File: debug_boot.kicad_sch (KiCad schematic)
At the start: 11 parts, among them J3 Conn_ARM_JTAG_SWD_10, J4 Conn_01x03, J5 Conn_01x05, J6 Conn_01x03, J8 DE9_Pins

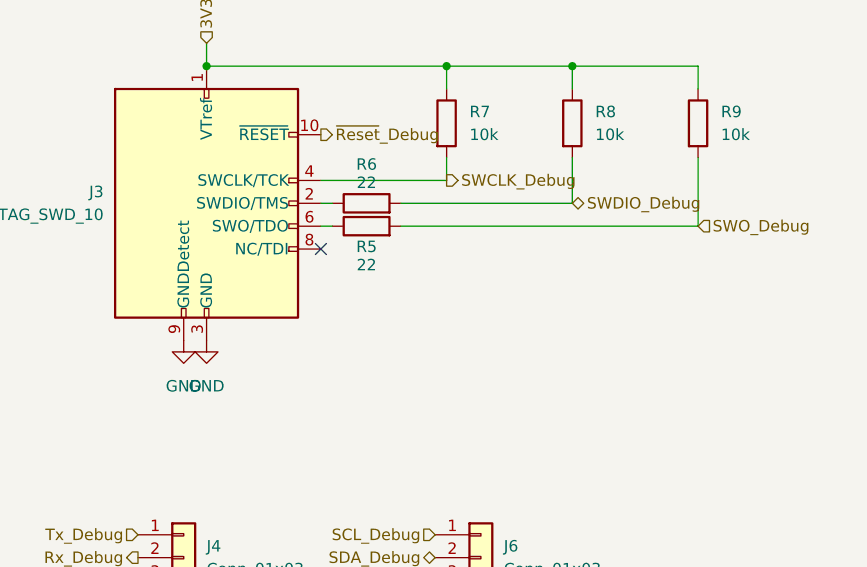
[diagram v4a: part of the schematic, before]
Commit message: Add crystal oscillator and button for reset
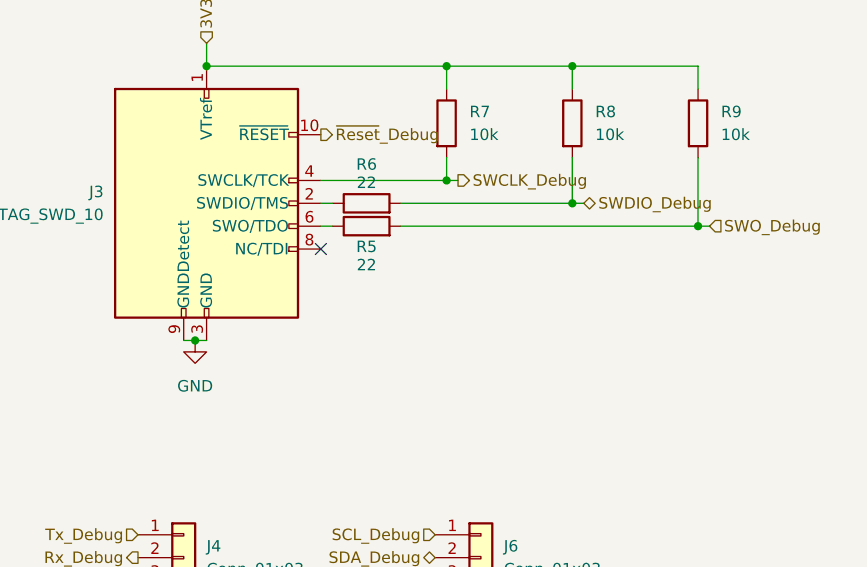
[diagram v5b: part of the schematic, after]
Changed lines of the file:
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@@
+	)
+	(junction
+		(at 172.72 69.85)
+		(diameter 0)
+		(color 0 0 0 0)
 	)
 	(junction
@@
 	)
 	(junction
+		(at 186.69 72.39)
+		(diameter 0)
+		(color 0 0 0 0)
+	)
+	(junction
+		(at 158.75 67.31)
+		(diameter 0)
+		(color 0 0 0 0)
+	)
+	(junction
 		(at 168.91 134.62)
 		(diameter 0)
@@
 	)
 	(junction
+		(at 130.81 85.09)
+		(diameter 0)
+		(color 0 0 0 0)
+	)
+	(junction
 		(at 158.75 54.61)
 		(diameter 0)
@@
 	(wire
 		(pts
+			(xy 172.72 69.85) (xy 172.72 64.77)
+		)
+		(stroke
+			(width 0)
+			(type default)
+		)
+	)
+	(wire
+		(pts
+			(xy 158.75 67.31) (xy 160.02 67.31)
+		)
+		(stroke
+			(width 0)
+			(type default)
+		)
+	)
+	(wire
+		(pts
 			(xy 158.75 54.61) (xy 172.72 54.61)
 		)
@@
 	(wire
 		(pts
+			(xy 162.56 144.78) (xy 168.91 144.78)
+		)
+		(stroke
+			(width 0)
+			(type default)
+		)
+	)
+	(wire
+		(pts
+			(xy 158.75 64.77) (xy 158.75 67.31)
+		)
+		(stroke
+			(width 0)
+			(type default)
+		)
+	)
+	(wire
+		(pts
+			(xy 168.91 144.78) (xy 171.45 144.78)
+		)
+		(stroke
+			(width 0)
+			(type default)
+		)
+	)
+	(wire
+		(pts
+			(xy 168.91 143.51) (xy 168.91 144.78)
+		)
+		(stroke
+			(width 0)
+			(type default)
+		)
+	)
+	(wire
+		(pts
+			(xy 187.96 72.39) (xy 186.69 72.39)
+		)
+		(stroke
+			(width 0)
+			(type default)
+		)
+	)
+	(wire
+		(pts
+			(xy 162.56 134.62) (xy 168.91 134.62)
+		)
+		(stroke
+			(width 0)
+			(type default)
+		)
+	)
+	(wire
+		(pts
+			(xy 132.08 52.07) (xy 132.08 54.61)
+		)
+		(stroke
+			(width 0)
+			(type default)
+		)
+	)
+	(wire
+		(pts
+			(xy 158.75 67.31) (xy 144.78 67.31)
+		)
+		(stroke
+			(width 0)
+			(type default)
+		)
+	)
+	(wire
+		(pts
+			(xy 186.69 72.39) (xy 186.69 64.77)
+		)
+		(stroke
+			(width 0)
+			(type default)
+		)
+	)
+	(wire
+		(pts
+			(xy 171.45 138.43) (xy 180.34 138.43)
+		)
+		(stroke
+			(width 0)
+			(type default)
+		)
+	)
+	(wire
+		(pts
+			(xy 172.72 54.61) (xy 186.69 54.61)
+		)
+		(stroke
+			(width 0)
+			(type default)
+		)
+	)
+	(wire
+		(pts
+			(xy 158.75 54.61) (xy 158.75 57.15)
+		)
+		(stroke
+			(width 0)
+			(type default)
+		)
+	)
+	(wire
+		(pts
+			(xy 130.81 85.09) (xy 129.54 85.09)
+		)
+		(stroke
+			(width 0)
+			(type default)
+		)
+	)
+	(wire
+		(pts
+			(xy 171.45 144.78) (xy 171.45 140.97)
+		)
+		(stroke
+			(width 0)
+			(type default)
+		)
+	)
+	(wire
+		(pts
 			(xy 172.72 69.85) (xy 153.67 69.85)
 		)
@@
 	(wire
 		(pts
-			(xy 186.69 72.39) (xy 186.69 64.77)
-		)
-		(stroke
-			(width 0)
-			(type default)
-		)
-	)
-	(wire
-		(pts
-			(xy 162.56 144.78) (xy 168.91 144.78)
-		)
-		(stroke
-			(width 0)
-			(type default)
-		)
-	)
-	(wire
-		(pts
-			(xy 158.75 64.77) (xy 158.75 67.31)
-		)
-		(stroke
-			(width 0)
-			(type default)
-		)
-	)
-	(wire
-		(pts
-			(xy 168.91 144.78) (xy 171.45 144.78)
-		)
-		(stroke
-			(width 0)
-			(type default)
-		)
-	)
-	(wire
-		(pts
-			(xy 168.91 143.51) (xy 168.91 144.78)
-		)
-		(stroke
-			(width 0)
-			(type default)
-		)
-	)
-	(wire
-		(pts
-			(xy 162.56 134.62) (xy 168.91 134.62)
-		)
-		(stroke
-			(width 0)
-			(type default)
-		)
-	)
-	(wire
-		(pts
-			(xy 132.08 52.07) (xy 132.08 54.61)
-		)
-		(stroke
-			(width 0)
-			(type default)
-		)
-	)
-	(wire
-		(pts
-			(xy 158.75 67.31) (xy 144.78 67.31)
-		)
-		(stroke
-			(width 0)
-			(type default)
-		)
-	)
-	(wire
-		(pts
-			(xy 171.45 138.43) (xy 180.34 138.43)
-		)
-		(stroke
-			(width 0)
-			(type default)
-		)
-	)
-	(wire
-		(pts
-			(xy 172.72 54.61) (xy 186.69 54.61)
-		)
-		(stroke
-			(width 0)
-			(type default)
-		)
-	)
-	(wire
-		(pts
-			(xy 158.75 54.61) (xy 158.75 57.15)
-		)
-		(stroke
-			(width 0)
-			(type default)
-		)
-	)
-	(wire
-		(pts
-			(xy 171.45 144.78) (xy 171.45 140.97)
-		)
-		(stroke
-			(width 0)
-			(type default)
-		)
-	)
-	(wire
-		(pts
 			(xy 132.08 54.61) (xy 158.75 54.61)
 		)
@@
 	(wire
 		(pts
+			(xy 130.81 85.09) (xy 132.08 85.09)
+		)
+		(stroke
+			(width 0)
+			(type default)
+		)
+	)
+	(wire
+		(pts
 			(xy 144.78 69.85) (xy 146.05 69.85)
 		)
@@
 	(wire
 		(pts
-			(xy 172.72 69.85) (xy 172.72 64.77)
+			(xy 173.99 69.85) (xy 172.72 69.85)
 		)
 		(stroke
@@
 	(hierarchical_label "SWDIO_Debug"
 		(shape bidirectional)
-		(at 172.72 69.85 0)
+		(at 173.99 69.85 0)
 		(effects
 			(font
@@
 	(hierarchical_label "SWO_Debug"
 		(shape input)
-		(at 186.69 72.39 0)
+		(at 187.96 72.39 0)
 		(effects
 			(font
@@
 	(hierarchical_label "SWCLK_Debug"
 		(shape output)
-		(at 158.75 67.31 0)
+		(at 160.02 67.31 0)
 		(effects
 			(font
@@
 	(symbol
 		(lib_id "power:GND")
-		(at 132.08 85.09 0)
-		(unit 1)
-		(exclude_from_sim no)
-		(in_bom yes)
-		(on_board yes)
-		(dnp no)
-		(fields_autoplaced yes)
-		(property "Reference" "#PWR030"
-			(at 132.08 91.44 0)
-			(effects
-				(font
-					(size 1.27 1.27)
-				)
-				(hide yes)
-			)
-		)
-		(property "Value" "GND"
-			(at 132.08 90.17 0)
-			(effects
-				(font
-					(size 1.27 1.27)
-				)
-			)
-		)
-		(property "Footprint" ""
-			(at 132.08 85.09 0)
-			(effects
-				(font
-					(size 1.27 1.27)
-				)
-				(hide yes)
-			)
-		)
-		(property "Datasheet" ""
-			(at 132.08 85.09 0)
-			(effects
-				(font
-					(size 1.27 1.27)
-				)
-				(hide yes)
-			)
-		)
-		(property "Description" "Power symbol creates a global label with name \"GND\" , ground"
-			(at 132.08 85.09 0)
-			(effects
-				(font
-					(size 1.27 1.27)
-				)
-				(hide yes)
-			)
-		)
-		(pin "1"
-		)
-		(instances
-			(project "weather-station-poc"
-				(path "/38eb53bb-294e-46e4-ad59-fd355ca373b9/8a588a02-5ba4-4712-b770-7d9eb4e5d127"
-					(reference "#PWR030")
-					(unit 1)
-				)
-			)
-		)
-	)
-	(symbol
-		(lib_id "power:GND")
-		(at 129.54 85.09 0)
+		(at 130.81 85.09 0)
 		(unit 1)
 		(exclude_from_sim no)
@@
 		(fields_autoplaced yes)
 		(property "Reference" "#PWR029"
-			(at 129.54 91.44 0)
+			(at 130.81 91.44 0)
 			(effects
 				(font
@@
 		)
 		(property "Value" "GND"
-			(at 129.54 90.17 0)
+			(at 130.81 90.17 0)
 			(effects
 				(font
@@
 		)
 		(property "Footprint" ""
-			(at 129.54 85.09 0)
+			(at 130.81 85.09 0)
 			(effects
 				(font
@@
 		)
 		(property "Datasheet" ""
-			(at 129.54 85.09 0)
+			(at 130.81 85.09 0)
 			(effects
 				(font
@@
 		)
 		(property "Description" "Power symbol creates a global label with name \"GND\" , ground"
-			(at 129.54 85.09 0)
-			(effects
-				(font
+			(at 130.81 85.09 0)
+			(effects
+				(font

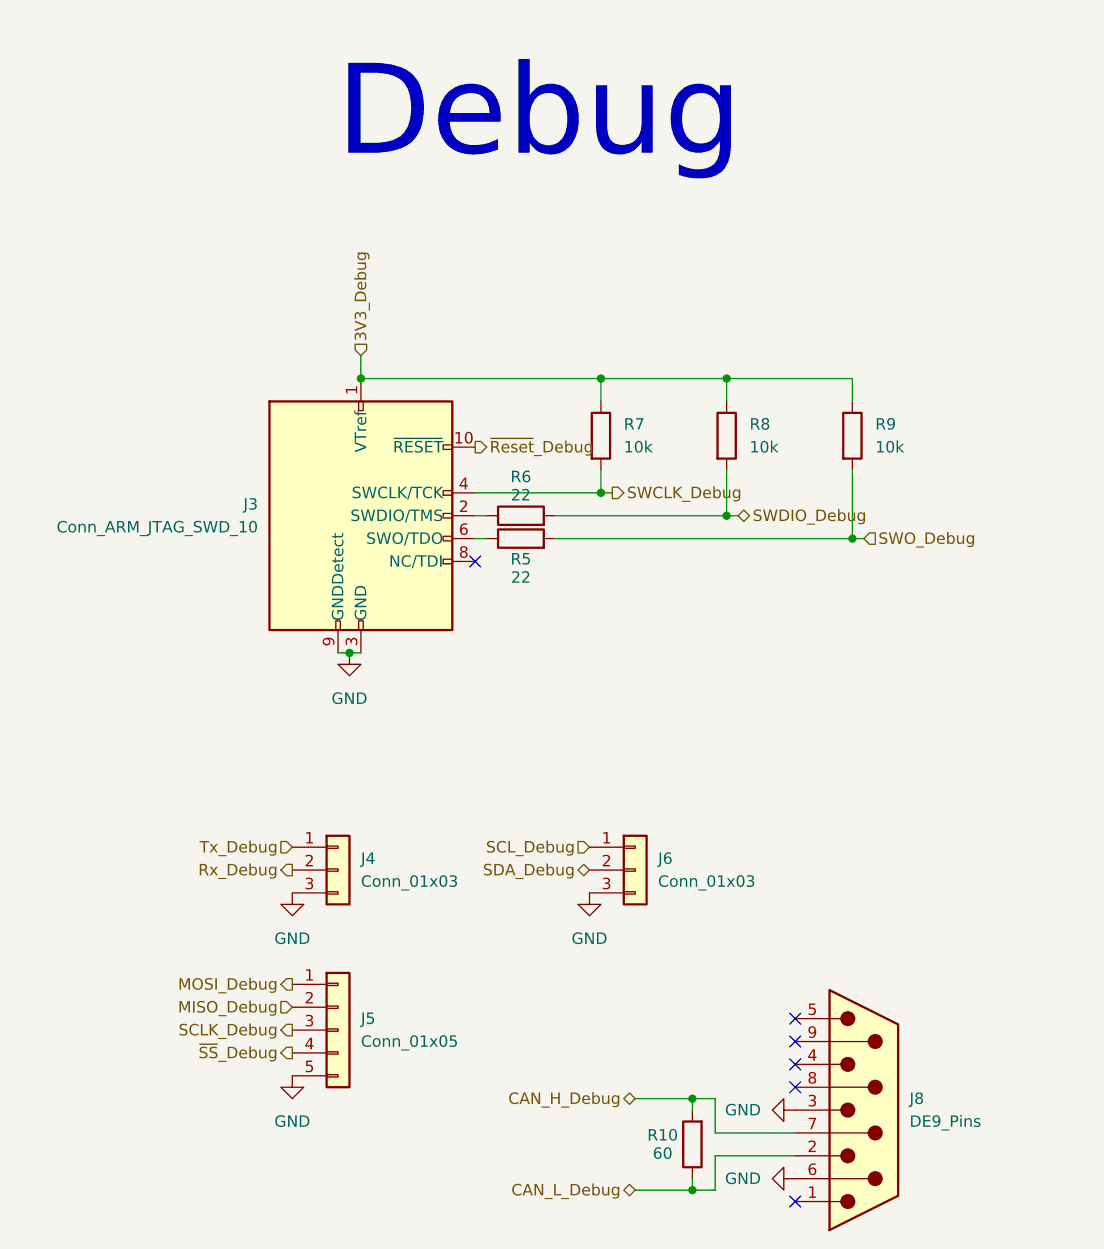
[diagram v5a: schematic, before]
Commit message: Functionnal block delimiting in schematics
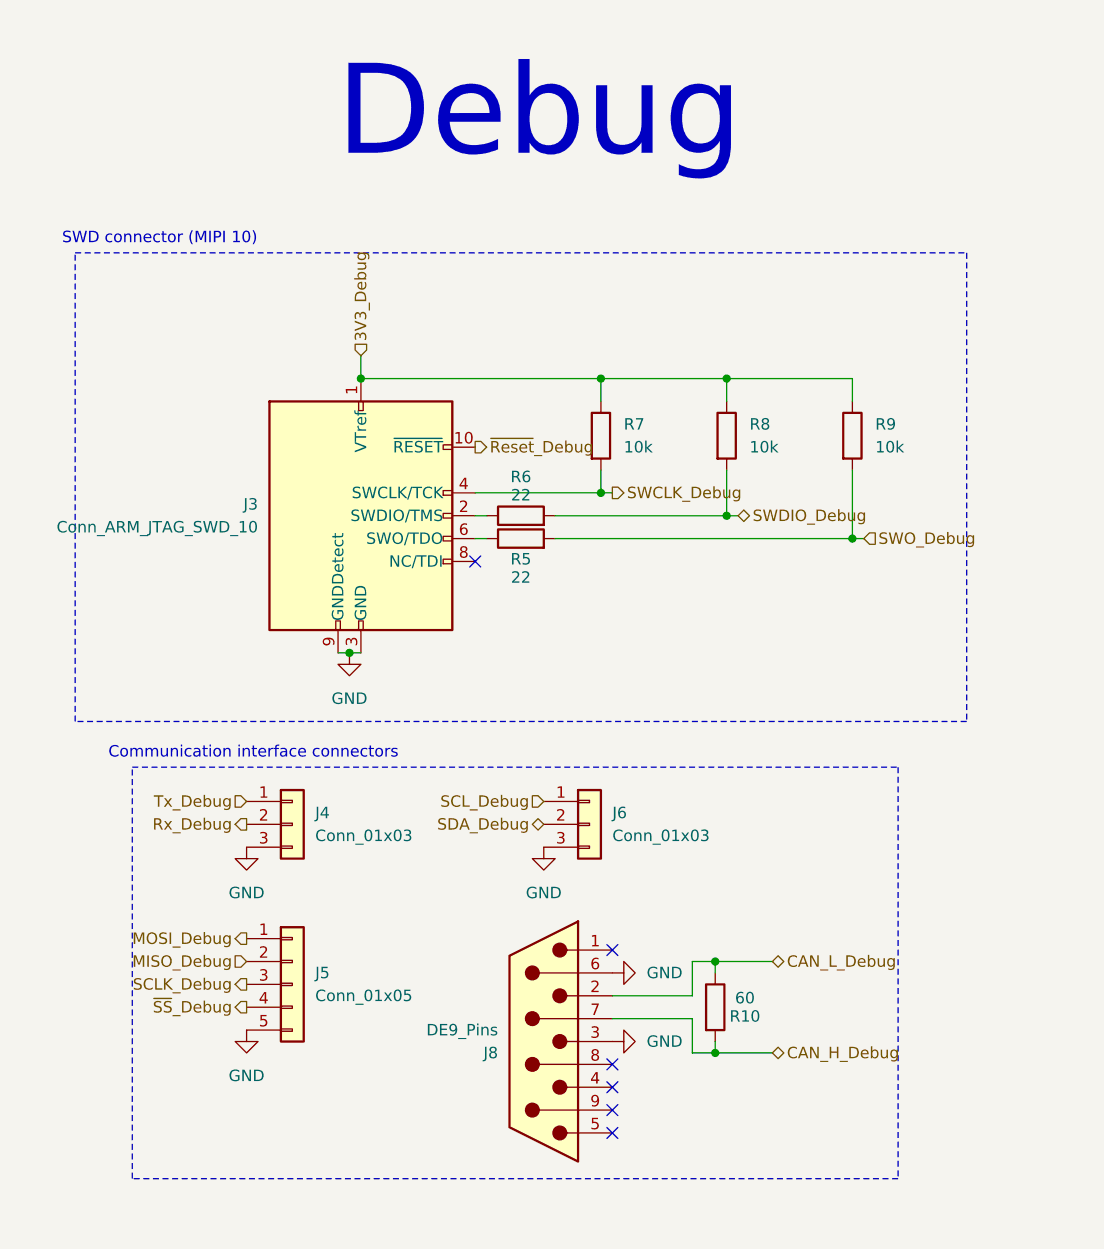
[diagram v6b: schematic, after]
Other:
- note added: "Communication interface connectors"
- note added: "SWD connector (MIPI 10)"
- moved on the sheet: J4, J5, J6, J8, R10

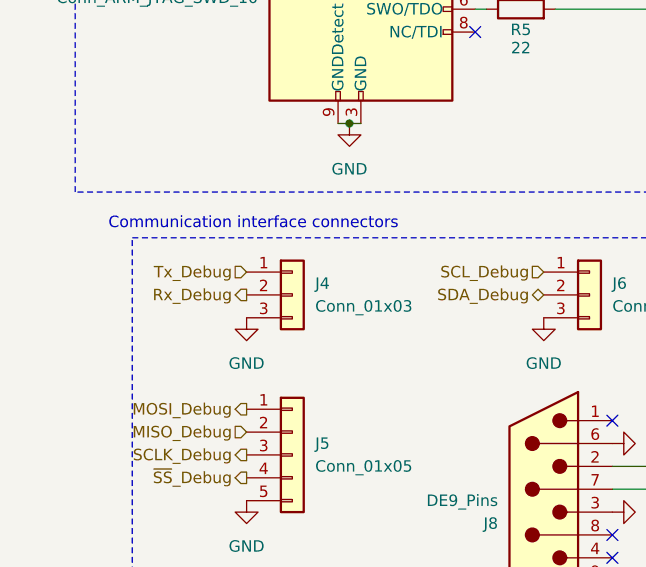
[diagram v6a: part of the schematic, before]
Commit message: Fix errors in synoptic and hierarchic pins
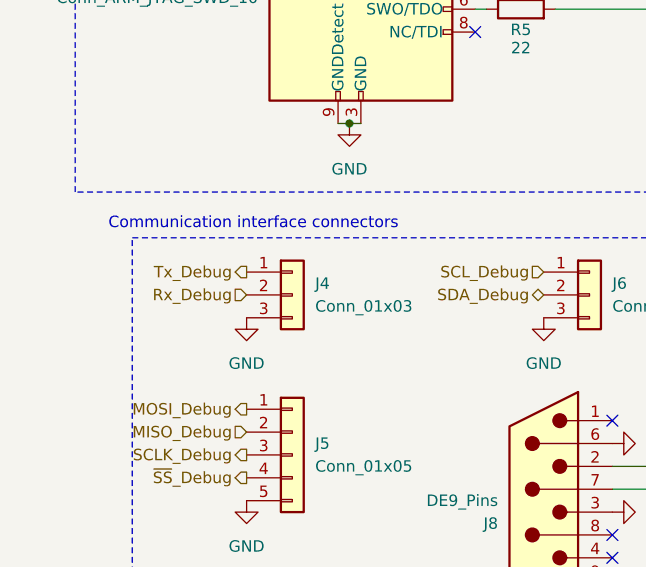
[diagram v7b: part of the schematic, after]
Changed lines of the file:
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@@
 	)
 	(hierarchical_label "Rx_Debug"
-		(shape output)
+		(shape input)
 		(at 119.38 104.14 180)
 		(effects
@@
 	)
 	(hierarchical_label "Tx_Debug"
-		(shape input)
+		(shape output)
 		(at 119.38 101.6 180)
 		(effects

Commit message: Continue schematic review
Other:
- note added: "TODO: Sub d 9pts connector is very big on a PCB, maybe replace by a pin header"
- note added: "TODO: see what resistor set on SWD"
- moved on the sheet: R7, R8, R9
